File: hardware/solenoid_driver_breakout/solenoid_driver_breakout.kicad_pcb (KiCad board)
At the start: 2 copper layers, 40 x 30 mm, 24 parts, among them J1 DC IN, J2 CONTROL, J3 Solenoid, Q1 PMV40UN2R, Q2 PMV40UN2R

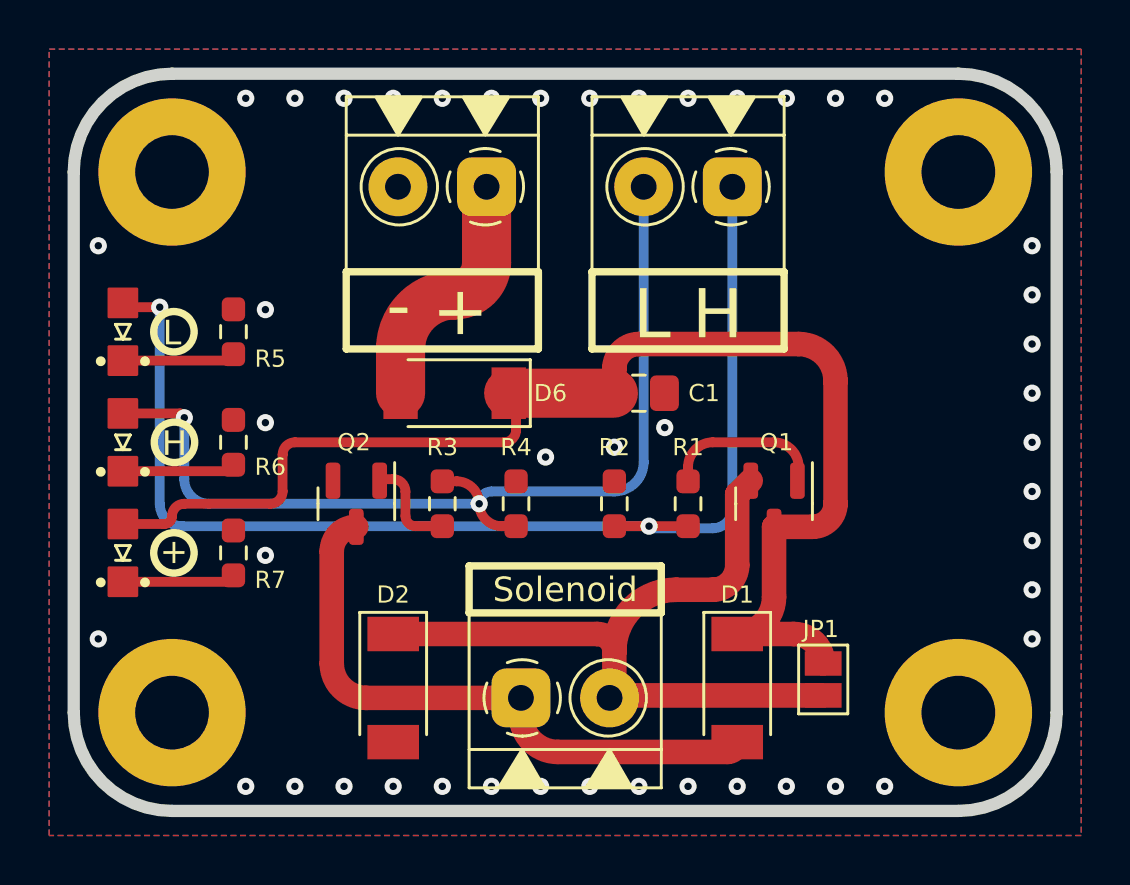
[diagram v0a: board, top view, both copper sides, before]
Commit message: Switch solenoid driver to dual low-side switches
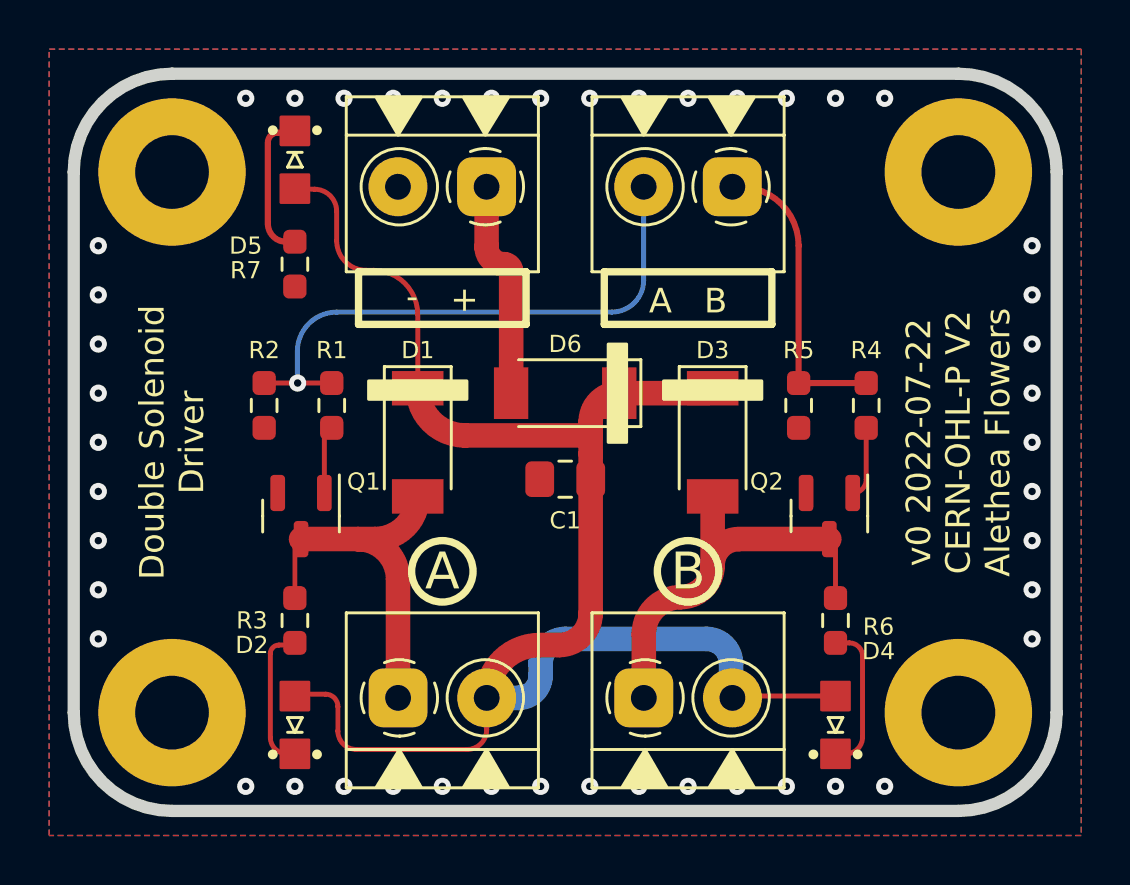
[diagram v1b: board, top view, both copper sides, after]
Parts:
- removed JP1: LOWSIDE ONLY, Jumper:SolderJumper-2_P1.3mm_Open_Pad1.0x1.5mm
- added G***: LOGO, winterbloom:Symbol_Winterbloom_25mm, B.Cu at (88.3, 99.9)
- added J4: Solenoid B, winterbloom:TerminalBlock_4UCON_1x02_P3.50mm_Horizontal, F.Cu at (92.8, 104.5)
- D1: value PMEG3030EP,115 -> 30V 1A
- D2: value PMEG3030EP,115 -> A; footprint Diode_SMD:D_SOD-128 -> winterbloom:LED_0805_Kingbright_APT2012
- D3: value H -> 30V 1A; footprint winterbloom:LED_0805_Kingbright_APT2012 -> Diode_SMD:D_SOD-128
- D4: value L -> A
- D6: value PMEG3030EP,115 -> 30V 2A
- J3: value Solenoid -> Solenoid A
- R3: value 1K -> 10K
- R4: value 100K -> 1K
- R5: value 5K1 -> 100K
- R6: value 5K1 -> 10K
- moved D4 31.2 mm to (100.5, 105.6)
- moved R6 25.6 mm to (100.5, 101.3)
- moved D3 24.4 mm to (95.5, 94.1), turned to -90 degrees
- moved R5 23.2 mm to (99.0, 92.6), turned to -90 degrees
- moved Q1 19.3 mm to (78.8, 97.1)
- moved Q2 19.3 mm to (100.2, 97.1)
- moved D5 17.5 mm to (78.5, 82.6), turned to -90 degrees
- moved D1 16.4 mm to (83.5, 94.1)
- moved R1 15.0 mm to (80.0, 92.6), turned to -90 degrees
- moved R2 14.8 mm to (77.2, 92.6), turned to -90 degrees
- moved R4 14.8 mm to (101.8, 92.6), turned to -90 degrees
- moved R7 12.0 mm to (78.5, 86.8), turned to -90 degrees
- moved R3 7.65 mm to (78.5, 101.3), turned to 90 degrees
- moved J3 5.00 mm to (82.8, 104.5)
- moved C1 4.61 mm to (89.5, 95.6), turned to 180 degrees
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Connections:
- net Net-(J1-Pad1) renamed /DCIN
- D1 pad 2: Net-(Q2-Pad3) -> /Switched A
- D2 pad 1: Net-(Q1-Pad2) -> Net-(D2-Pad1)
- D2 pad 2: GND -> +VDC
- D3 pad 1: Net-(D3-Pad1) -> +VDC
- D3 pad 2: /H -> /Switched B
- D4 pad 2: /L -> +VDC
- J2 pad 1: /H -> /Control B
- J2 pad 2: /L -> /Control A
- J3 pad 1: Net-(Q2-Pad3) -> /Switched A
- J3 pad 2: Net-(Q1-Pad2) -> +VDC
- Q1 pad 2: Net-(Q1-Pad2) -> GND
- Q1 pad 3: +VDC -> /Switched A
- Q2 pad 1: Net-(Q2-Pad1) -> Net-(R4-Pad2)
- Q2 pad 3: Net-(Q2-Pad3) -> /Switched B
- R1 pad 1: /H -> /Control A
- R2 pad 1: /H -> /Control A
- R3 pad 1: /L -> Net-(D2-Pad1)
- R3 pad 2: Net-(Q2-Pad1) -> /Switched A
- R4 pad 1: /L -> /Control B
- R4 pad 2: GND -> Net-(R4-Pad2)
- R5 pad 1: Net-(D3-Pad1) -> /Control B
- R6 pad 2: GND -> /Switched B
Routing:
- net /H: track 49.9 -> 0.00 mm, vias 2 -> 0
- net /L: track 40.4 -> 0.00 mm, vias 2 -> 0
- net Net-(Q1-Pad2): track 30.6 -> 0.00 mm
- net Net-(Q2-Pad3): track 25.0 -> 0.00 mm
- net /Control A: track 0.00 -> 23.5 mm, vias 0 -> 1
- net /Switched B: track 0.00 -> 17.5 mm
- net /Switched A: track 0.00 -> 15.5 mm
- net +VDC: track 53.3 -> 67.1 mm
- net /Control B: track 0.00 -> 12.0 mm
- net Net-(D2-Pad1): track 0.00 -> 5.53 mm
- net Net-(D3-Pad1): track 4.64 -> 0.00 mm
- net Net-(Q1-Pad1): track 6.74 -> 2.35 mm
- net Net-(Q2-Pad1): track 4.07 -> 0.00 mm
- net Net-(R4-Pad2): track 0.00 -> 2.94 mm
- net Net-(D5-Pad1): track 4.64 -> 6.03 mm
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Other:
- board text added: "${REVISION} ${ISSUE_DATE} ${COMMENT2} ${COMMENT1}"
- board text added: "A"
- board text added: "A B"
- board text added: "B"
- board text added: "Double Solenoid Driver"
- board text added: "Vin = 24V Vg = 3.3 V / 5 V Id = 300 mA"
- board text removed: "${TITLE} ${REVISION} ${ISSUE_DATE} ${COMMENT2} ${COMMENT1}"
- board text removed: "+"
- board text removed: "H"
- board text removed: "L"
- board text removed: "L H"

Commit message: Add smart solenoid drivers
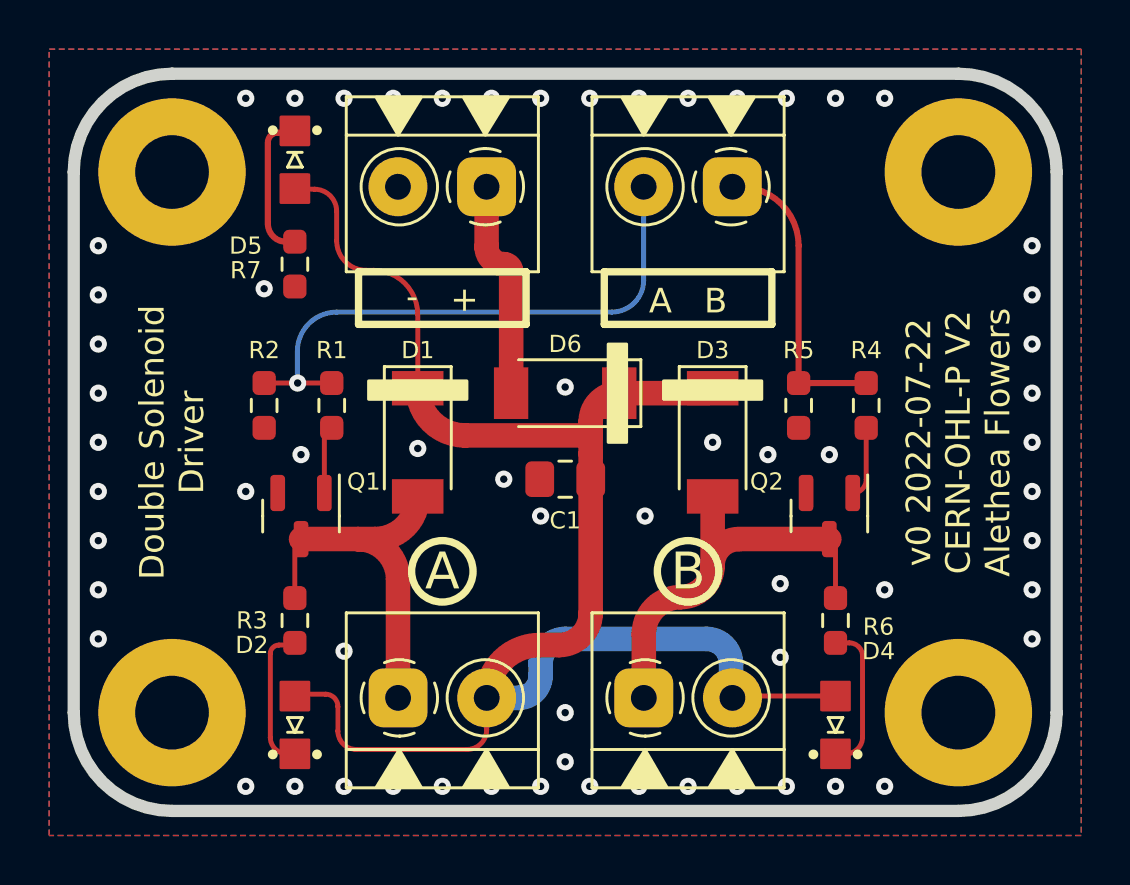
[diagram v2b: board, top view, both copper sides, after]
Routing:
- net GND: vias 46 -> 63
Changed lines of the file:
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@@
   (via (at 98.5 108.075) (size 0.7) (drill 0.3) (layers "F.Cu" "B.Cu") (free) (net 1))
   (via (at 84.5 108.075) (size 0.7) (drill 0.3) (layers "F.Cu" "B.Cu") (free) (net 1))
+  (via (at 80.5 102.575) (size 0.7) (drill 0.3) (layers "F.Cu" "B.Cu") (free) (net 1))
   (via (at 70.5 94.075) (size 0.7) (drill 0.3) (layers "F.Cu" "B.Cu") (free) (net 1))
   (via (at 98.5 80.075) (size 0.7) (drill 0.3) (layers "F.Cu" "B.Cu") (free) (net 1))
   (via (at 70.5 90.075) (size 0.7) (drill 0.3) (layers "F.Cu" "B.Cu") (free) (net 1))
+  (via (at 98.25 102.825) (size 0.7) (drill 0.3) (layers "F.Cu" "B.Cu") (free) (net 1))
   (via (at 94.5 80.075) (size 0.7) (drill 0.3) (layers "F.Cu" "B.Cu") (free) (net 1))
+  (via (at 97.75 94.575) (size 0.7) (drill 0.3) (layers "F.Cu" "B.Cu") (free) (net 1))
+  (via (at 83.5 94.325) (size 0.7) (drill 0.3) (layers "F.Cu" "B.Cu") (free) (net 1))
   (via (at 102.5 108.075) (size 0.7) (drill 0.3) (layers "F.Cu" "B.Cu") (free) (net 1))
   (via (at 70.5 98.075) (size 0.7) (drill 0.3) (layers "F.Cu" "B.Cu") (free) (net 1))
   (via (at 70.5 96.075) (size 0.7) (drill 0.3) (layers "F.Cu" "B.Cu") (free) (net 1))
+  (via (at 78.75 94.575) (size 0.7) (drill 0.3) (layers "F.Cu" "B.Cu") (free) (net 1))
+  (via (at 95.5 94.075) (size 0.7) (drill 0.3) (layers "F.Cu" "B.Cu") (free) (net 1))
+  (via (at 87 95.575) (size 0.7) (drill 0.3) (layers "F.Cu" "B.Cu") (free) (net 1))
   (via (at 86.5 108.075) (size 0.7) (drill 0.3) (layers "F.Cu" "B.Cu") (free) (net 1))
   (via (at 90.5 80.075) (size 0.7) (drill 0.3) (layers "F.Cu" "B.Cu") (free) (net 1))
   (via (at 76.5 80.075) (size 0.7) (drill 0.3) (layers "F.Cu" "B.Cu") (free) (net 1))
+  (via (at 89.5 91.825) (size 0.7) (drill 0.3) (layers "F.Cu" "B.Cu") (free) (net 1))
   (via (at 108.5 88.075) (size 0.7) (drill 0.3) (layers "F.Cu" "B.Cu") (free) (net 1))
   (via (at 86.5 80.075) (size 0.7) (drill 0.3) (layers "F.Cu" "B.Cu") (free) (net 1))
@@
   (via (at 90.5 108.075) (size 0.7) (drill 0.3) (layers "F.Cu" "B.Cu") (free) (net 1))
   (via (at 92.5 108.075) (size 0.7) (drill 0.3) (layers "F.Cu" "B.Cu") (free) (net 1))
+  (via (at 88.5 97.075) (size 0.7) (drill 0.3) (layers "F.Cu" "B.Cu") (free) (net 1))
   (via (at 108.5 100.075) (size 0.7) (drill 0.3) (layers "F.Cu" "B.Cu") (free) (net 1))
   (via (at 70.5 92.075) (size 0.7) (drill 0.3) (layers "F.Cu" "B.Cu") (free) (net 1))
   (via (at 82.5 108.075) (size 0.7) (drill 0.3) (layers "F.Cu" "B.Cu") (free) (net 1))
+  (via (at 77.25 87.825) (size 0.7) (drill 0.3) (layers "F.Cu" "B.Cu") (free) (net 1))
   (via (at 94.5 108.075) (size 0.7) (drill 0.3) (layers "F.Cu" "B.Cu") (free) (net 1))
   (via (at 108.5 86.075) (size 0.7) (drill 0.3) (layers "F.Cu" "B.Cu") (free) (net 1))
@@
   (via (at 70.5 102.075) (size 0.7) (drill 0.3) (layers "F.Cu" "B.Cu") (free) (net 1))
   (via (at 88.5 108.075) (size 0.7) (drill 0.3) (layers "F.Cu" "B.Cu") (free) (net 1))
+  (via (at 100.25 94.575) (size 0.7) (drill 0.3) (layers "F.Cu" "B.Cu") (free) (net 1))
   (via (at 100.5 80.075) (size 0.7) (drill 0.3) (layers "F.Cu" "B.Cu") (free) (net 1))
+  (via (at 89.5 107.075) (size 0.7) (drill 0.3) (layers "F.Cu" "B.Cu") (free) (net 1))
   (via (at 78.5 108.075) (size 0.7) (drill 0.3) (layers "F.Cu" "B.Cu") (free) (net 1))
+  (via (at 76.5 96.075) (size 0.7) (drill 0.3) (layers "F.Cu" "B.Cu") (free) (net 1))
+  (via (at 92.75 97.075) (size 0.7) (drill 0.3) (layers "F.Cu" "B.Cu") (free) (net 1))
+  (via (at 98.25 99.825) (size 0.7) (drill 0.3) (layers "F.Cu" "B.Cu") (free) (net 1))
   (via (at 78.5 80.075) (size 0.7) (drill 0.3) (layers "F.Cu" "B.Cu") (free) (net 1))
   (via (at 82.5 80.075) (size 0.7) (drill 0.3) (layers "F.Cu" "B.Cu") (free) (net 1))
   (via (at 100.5 108.075) (size 0.7) (drill 0.3) (layers "F.Cu" "B.Cu") (free) (net 1))
+  (via (at 102.5 100.075) (size 0.7) (drill 0.3) (layers "F.Cu" "B.Cu") (free) (net 1))
   (via (at 108.5 94.075) (size 0.7) (drill 0.3) (layers "F.Cu" "B.Cu") (free) (net 1))
   (via (at 70.5 86.075) (size 0.7) (drill 0.3) (layers "F.Cu" "B.Cu") (free) (net 1))
   (via (at 92.5 80.075) (size 0.7) (drill 0.3) (layers "F.Cu" "B.Cu") (free) (net 1))
+  (via (at 89.5 105.075) (size 0.7) (drill 0.3) (layers "F.Cu" "B.Cu") (free) (net 1))
   (via (at 102.5 80.075) (size 0.7) (drill 0.3) (layers "F.Cu" "B.Cu") (free) (net 1))
   (segment (start 77.4 85.175) (end 77.4 81.875) (width 0.25) (layer "F.Cu") (net 2))
